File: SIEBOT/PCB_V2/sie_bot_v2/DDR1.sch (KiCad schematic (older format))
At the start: 19 parts, among them U2 MT46V32M16TG, U3 M25P32

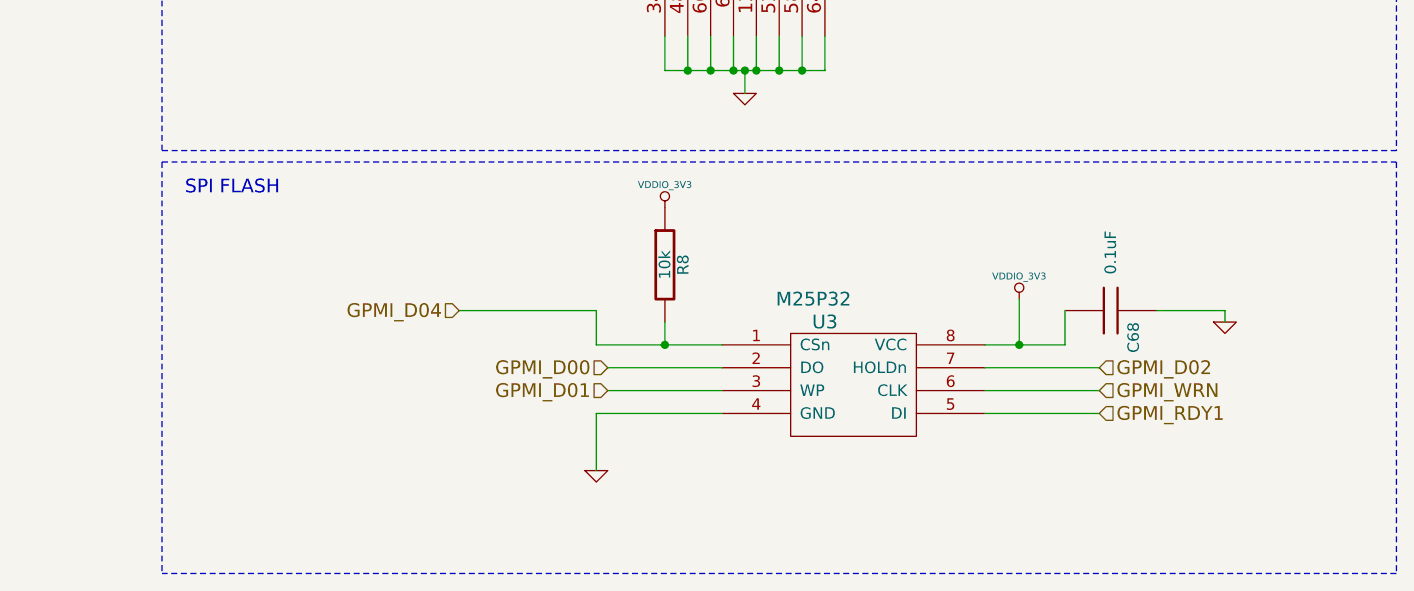
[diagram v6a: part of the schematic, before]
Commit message: Adición de r48 y r49 para llevar DO3 chip_select a la sd o a la memoria SPI
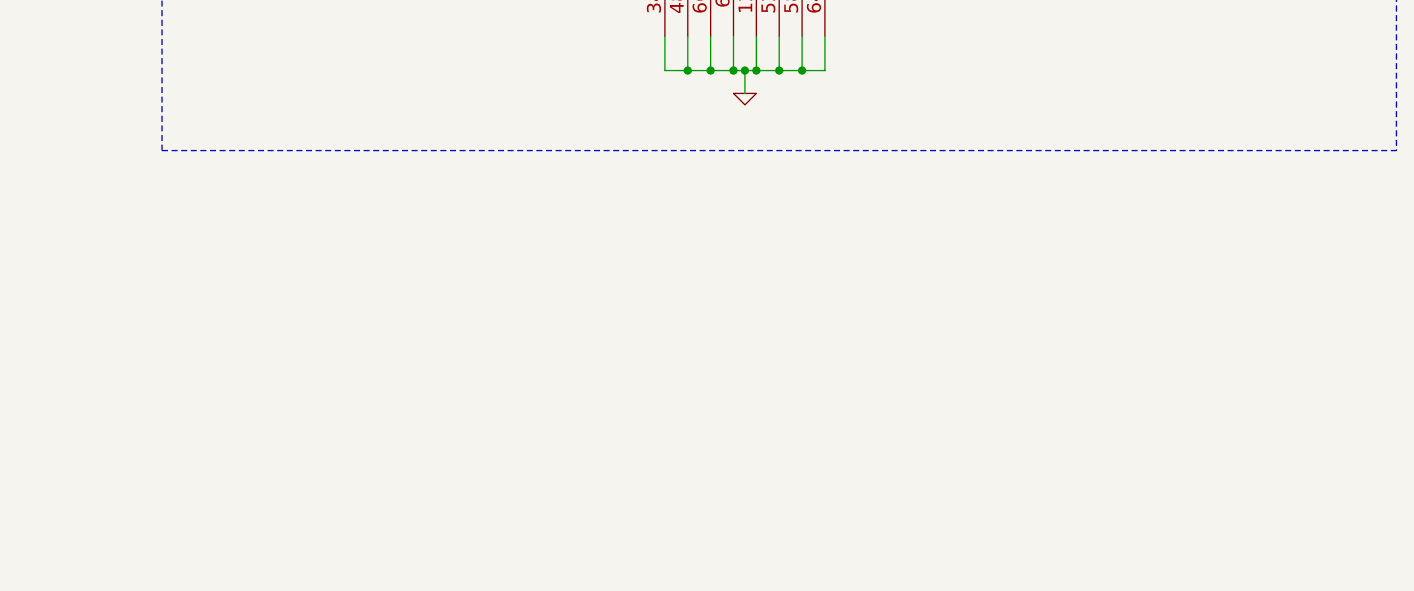
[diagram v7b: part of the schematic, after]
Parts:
- removed C68: 0.1uF, symbol C
- removed R8: 10k, symbol R
- removed U3: M25P32, SO16W, symbol M25P32
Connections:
- net labels removed: GPMI_D00, GPMI_D01, GPMI_D02, GPMI_D04, GPMI_RDY1, GPMI_WRN, VDDIO_3V3
- wire segments 138 -> 122
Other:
- note removed: "SPI FLASH"
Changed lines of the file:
@@
-EESchema Schematic File Version 2  date Fri 17 Feb 2012 07:53:32 PM COT
+EESchema Schematic File Version 2  date Sat 18 Feb 2012 11:36:23 AM COT
 LIBS:con-jack
 LIBS:adm3101e
@@
 Sheet 4 5
 Title ""
-Date "17 feb 2012"
+Date "18 feb 2012"
 Rev ""
 Comp ""
@@
 	8650 4950 7950 4950
 Wire Wire Line
-	7650 6150 7650 6000
-Wire Wire Line
-	7650 6150 8200 6150
-Connection ~ 7950 6150
-Wire Wire Line
-	7950 6050 7950 6150
-Wire Wire Line
 	5850 4500 5850 4300
 Wire Wire Line
 	6500 3900 7250 3900
-Wire Notes Line
-	5750 5350 5750 7150
 Wire Notes Line
 	5750 5300 11150 5300
@@
 Connection ~ 9600 950
 Connection ~ 9900 950
-Wire Wire Line
-	9850 6350 9350 6350
-Wire Wire Line
-	9700 6000 9700 6150
-Wire Wire Line
-	9700 6150 9350 6150
-Connection ~ 9500 6150
-Wire Wire Line
-	9500 5950 9500 6150
-Wire Wire Line
-	7700 6350 8200 6350
 Connection ~ 8550 1500
 Connection ~ 8350 1500
@@
 	8450 1500 8450 1600
 Connection ~ 8450 1500
-Wire Wire Line
-	7700 6250 8200 6250
-Wire Wire Line
-	8200 6450 7650 6450
-Wire Wire Line
-	7650 6450 7650 6700
-Wire Wire Line
-	10400 6050 10400 6000
-Wire Wire Line
-	10400 6000 10100 6000
-Wire Wire Line
-	9850 6250 9350 6250
-Wire Wire Line
-	9850 6450 9350 6450
 Connection ~ 9300 950
 Connection ~ 9900 1350
@@
 Wire Wire Line
 	2200 5700 2600 5700
-Wire Notes Line
-	5750 5350 11150 5350
-Wire Notes Line
-	11150 5350 11150 7150
-Wire Notes Line
-	11150 7150 5750 7150
 Wire Wire Line
 	5850 3800 7250 3800
-Wire Wire Line
-	7650 6000 7050 6000
-$Comp
-L VDDIO_3V3 #PWR099
-U 1 1 4D7E71FF
-P 7950 5550
-F 0 "#PWR099" H 7950 5650 30  0001 C CNN
-F 1 "VDDIO_3V3" H 7950 5650 30  0000 C CNN
-	1    7950 5550
-	1    0    0    -1
-$EndComp
-$Comp
-L R R8
-U 1 1 4D7E71FA
-P 7950 5800
-F 0 "R8" V 8030 5800 50  0000 C CNN
-F 1 "10k" V 7950 5800 50  0000 C CNN
-	1    7950 5800
-	1    0    0    -1
-$EndComp
-$Comp
-L VDDM_2V5 #PWR0100
+$Comp
+L VDDM_2V5 #PWR0103
 U 1 1 4D7E6BF9
 P 6000 3900
-F 0 "#PWR0100" H 6000 4000 30  0001 C CNN
+F 0 "#PWR0103" H 6000 4000 30  0001 C CNN
 F 1 "VDDM_2V5" H 5950 3950 30  0000 C CNN
 	1    6000 3900
@@
 	0    1    1    0
 $EndComp
-Text Notes 5850 5500 0    60   ~ 0
-SPI FLASH
 Text Notes 5850 750  0    60   ~ 0
 DDR RAM
@@
 $EndComp
 $Comp
-L GND #PWR0101
+L GND #PWR0104
 U 1 1 4D418353
 P 5850 4500
-F 0 "#PWR0101" H 5850 4500 30  0001 C CNN
+F 0 "#PWR0104" H 5850 4500 30  0001 C CNN
 F 1 "GND" H 5850 4430 30  0001 C CNN
 	1    5850 4500
@@
 DDR_CKE
 $Comp
-L GND #PWR0102
+L GND #PWR0105
 U 1 1 4D417AF1
 P 10800 2750
-F 0 "#PWR0102" H 10800 2750 30  0001 C CNN
+F 0 "#PWR0105" H 10800 2750 30  0001 C CNN
 F 1 "GND" H 10800 2680 30  0001 C CNN
 	1    10800 2750
@@
 $EndComp
 $Comp
-L VDDM_2V5 #PWR0103
+L VDDM_2V5 #PWR0106
 U 1 1 4D417ACD
 P 10800 1450
-F 0 "#PWR0103" H 10800 1550 30  0001 C CNN
+F 0 "#PWR0106" H 10800 1550 30  0001 C CNN
 F 1 "VDDM_2V5" H 10800 1550 30  0000 C CNN
 	1    10800 1450
@@
 $EndComp
 $Comp
-L VDDM_2V5 #PWR0104
+L VDDM_2V5 #PWR0107
 U 1 1 4D4179A4
 P 7250 800
-F 0 "#PWR0104" H 7250 900 30  0001 C CNN
+F 0 "#PWR0107" H 7250 900 30  0001 C CNN
 F 1 "VDDM_2V5" H 7250 900 30  0000 C CNN
 	1    7250 800
@@
 $EndComp
 $Comp
-L VDDM_2V5 #PWR0105
+L VDDM_2V5 #PWR0108
 U 1 1 4D417999
 P 10200 800
-F 0 "#PWR0105" H 10200 900 30  0001 C CNN
+F 0 "#PWR0108" H 10200 900 30  0001 C CNN
 F 1 "VDDM_2V5" H 10200 900 30  0000 C CNN
 	1    10200 800
@@
 $EndComp
 $Comp
-L GND #PWR0106
+L GND #PWR0109
 U 1 1 4D41792B
 P 7550 1500
-F 0 "#PWR0106" H 7550 1500 30  0001 C CNN
+F 0 "#PWR0109" H 7550 1500 30  0001 C CNN
 F 1 "GND" H 7550 1430 30  0001 C CNN
 	1    7550 1500
@@
 $EndComp
 $Comp
-L GND #PWR0107
+L GND #PWR0110
 U 1 1 4D417882
 P 9600 1500
-F 0 "#PWR0107" H 9600 1500 30  0001 C CNN
+F 0 "#PWR0110" H 9600 1500 30  0001 C CNN
 F 1 "GND" H 9600 1430 30  0001 C CNN
 	1    9600 1500
@@
 	1    0    0    -1
 $EndComp
-Text HLabel 9850 6250 2    60   Input ~ 0
-GPMI_D02
-Text HLabel 9850 6350 2    60   Input ~ 0
-GPMI_WRN
-Text HLabel 9850 6450 2    60   Input ~ 0
-GPMI_RDY1
-Text HLabel 7700 6350 0    60   Input ~ 0
-GPMI_D01
-Text HLabel 7700 6250 0    60   Input ~ 0
-GPMI_D00
-Text HLabel 7050 6000 0    60   Input ~ 0
-GPMI_D04
-$Comp
-L GND #PWR0108
-U 1 1 4D409664
-P 10400 6050
-F 0 "#PWR0108" H 10400 6050 30  0001 C CNN
-F 1 "GND" H 10400 5980 30  0001 C CNN
-	1    10400 6050
-	1    0    0    -1
-$EndComp
-$Comp
-L C C68
-U 1 1 4D409658
-P 9900 6000
-F 0 "C68" H 9950 6100 50  0000 L CNN
-F 1 "0.1uF" H 9550 6000 50  0000 L CNN
-	1    9900 6000
-	0    1    1    0
-$EndComp
-$Comp
-L VDDIO_3V3 #PWR0109
-U 1 1 4D409635
-P 9500 5950
-F 0 "#PWR0109" H 9500 6050 30  0001 C CNN
-F 1 "VDDIO_3V3" H 9500 6050 30  0000 C CNN
-	1    9500 5950
-	1    0    0    -1
-$EndComp
-$Comp
-L GND #PWR0110
-U 1 1 4D409619
-P 7650 6700
-F 0 "#PWR0110" H 7650 6700 30  0001 C CNN
-F 1 "GND" H 7650 6630 30  0001 C CNN
-	1    7650 6700
-	1    0    0    -1
-$EndComp
-$Comp
-L M25P32 U3
-U 1 1 4D40953F
-P 8800 6200
-F 0 "U3" H 8650 6350 60  0000 C CNN
-F 1 "M25P32" H 8600 6450 60  0000 C CNN
-F 2 "SO16W" H 8800 6200 60  0001 C CNN
-	1    8800 6200
-	1    0    0    -1
-$EndComp
